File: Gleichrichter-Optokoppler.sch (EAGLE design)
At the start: 9 parts, among them X2 22-23-2041

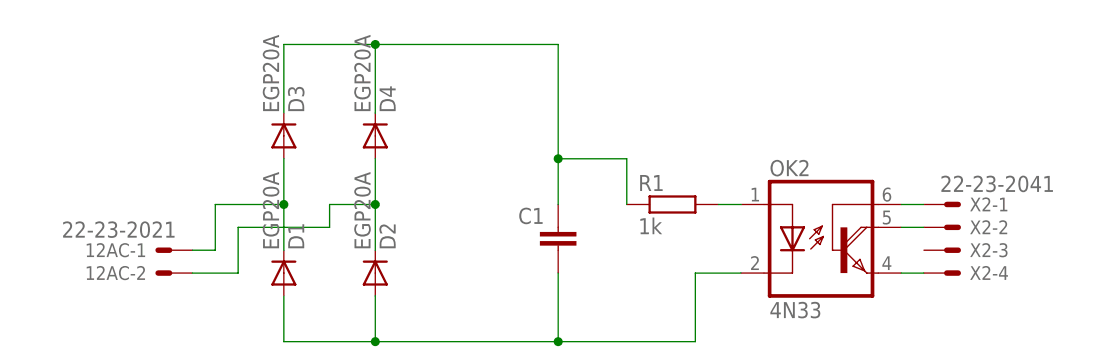
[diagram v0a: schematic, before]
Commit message: datasheet of 4N38A and powersupply text
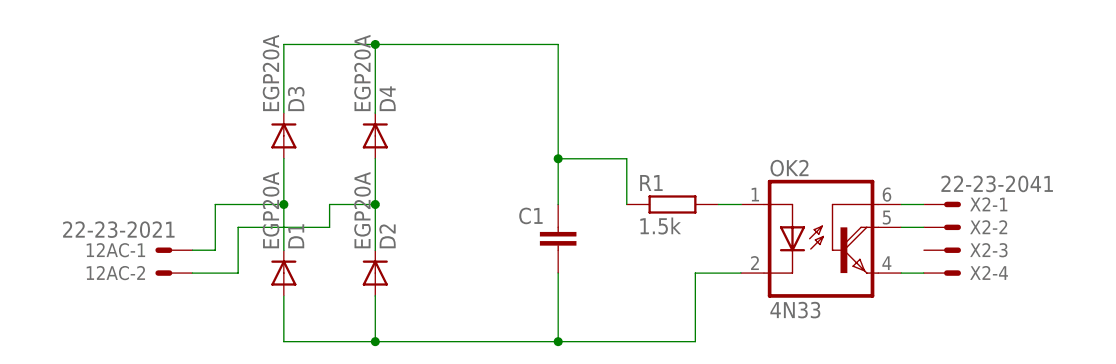
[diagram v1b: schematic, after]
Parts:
- R1: value 1k -> 1.5k
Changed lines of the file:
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@@
 </classes>
 <parts>
-<part name="R1" library="eagle-ltspice" deviceset="R" device="0207/10" value="1k"/>
+<part name="R1" library="eagle-ltspice" deviceset="R" device="0207/10" value="1.5k"/>
 <part name="C1" library="capacitor-wima" deviceset="C" device="5/4.5"/>
 <part name="D1" library="diode" deviceset="EGP20A" device=""/>
